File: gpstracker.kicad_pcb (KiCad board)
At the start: 2 copper layers, 79.2 x 59.2 mm, 193 parts, among them IC1 SIM808, J1 Molex 105133-0002, J2 Leds, J3 47553-0001, J4 CONN_COAXIAL, J5 CONN_COAXIAL, J6 Micro_SD_Card, Q1 DMP1045U, SW1 Reset, U1 MCP73832-5-OT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

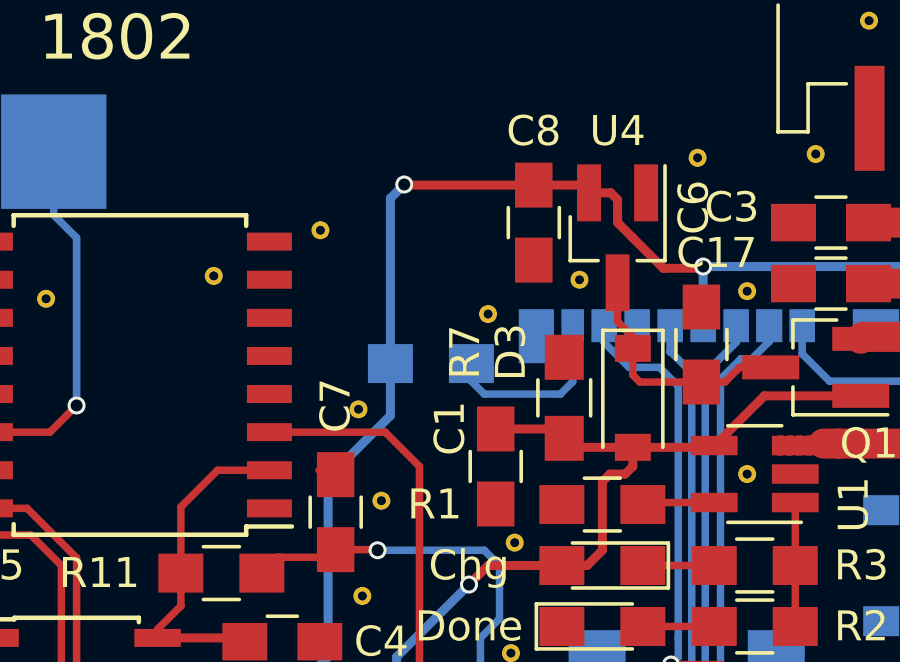
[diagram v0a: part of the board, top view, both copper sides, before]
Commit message: Move sd card right pull up resistor a bit avoid conflicts
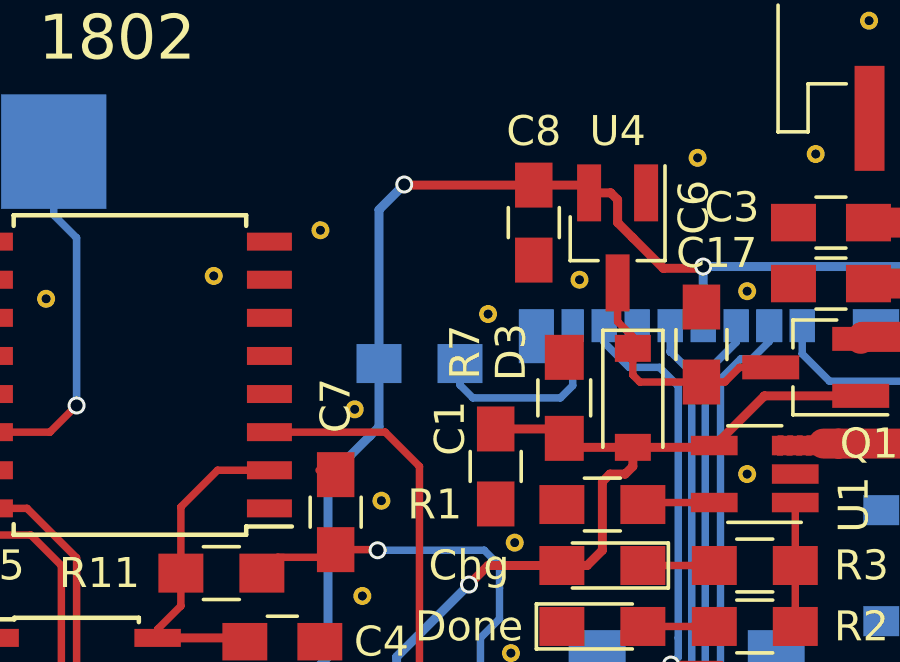
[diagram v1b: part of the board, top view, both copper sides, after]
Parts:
- moved R14 0.38 mm to (123.4, 85.2)
- moved VIA** 0.13 mm to (121.3, 86.7)
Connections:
- J6 pad 9: GND -> (no net)
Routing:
- net Net-(J6-Pad8): track 6.18 -> 6.82 mm
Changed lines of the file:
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@@
 (kicad_pcb (version 4) (host pcbnew 4.0.7)
   (general
-    (links 315)
+    (links 314)
     (no_connects 0)
     (area 76.986002 51.656 194.286 129.599)
     (thickness 1.6)
     (drawings 16)
-    (tracks 607)
+    (tracks 609)
     (zones 0)
     (modules 193)
@@
     (mod_text_size 1 1)
     (mod_text_width 0.15)
-    (pad_size 2.1 2.1)
-    (pad_drill 1.35)
+    (pad_size 1.2 1)
+    (pad_drill 0)
     (pad_to_mask_clearance 0.2)
     (aux_axis_origin 0 0)
@@
     (pad 1 smd rect (at 3.105 -5.2) (size 0.85 1.1) (layers B.Cu B.Paste B.Mask)
       (net 68 "Net-(J6-Pad1)"))
-    (pad 9 smd rect (at 5.74 0.95) (size 1.2 1) (layers B.Cu B.Paste B.Mask)
-      (net 2 GND))
+    (pad 9 smd rect (at 5.74 0.95) (size 1.2 1) (layers B.Cu B.Paste B.Mask))
     (pad 10 smd rect (at 5.74 4.65) (size 1.2 1) (layers B.Cu B.Paste B.Mask))
     (pad G3 smd rect (at -3.73 5.625) (size 1.9 1.35) (layers B.Cu B.Paste B.Mask))
@@
   )
   (module custom-conn:Via-0.6mm (layer F.Cu)
-    (at 121.412 86.741)
+    (at 121.285 86.741)
     (fp_text reference VIA** (at 0 1.27) (layer F.SilkS) hide
       (effects (font (size 1 1) (thickness 0.15)))
@@
   )
   (module Resistors_SMD:R_0805_HandSoldering (layer B.Cu)
-    (at 123.825 85.217 180)
+    (at 123.444 85.217 180)
     (descr "Resistor SMD 0805, hand soldering")
     (tags "resistor 0805")
@@
   (segment (start 129.94 98.366) (end 129.94 96.481) (width 0.25) (layer F.Cu) (net 5))
   (segment (start 129.94 96.481) (end 130.155 96.266) (width 0.25) (layer F.Cu) (net 5))
-  (segment (start 122.475 85.217) (end 122.475 86.948) (width 0.3) (layer B.Cu) (net 6))
-  (segment (start 122.475 86.948) (end 120.396 89.027) (width 0.3) (layer B.Cu) (net 6))
-  (segment (start 122.475 85.217) (end 122.475 79.709) (width 0.3) (layer B.Cu) (net 6))
-  (segment (start 122.475 79.709) (end 122.936 79.248) (width 0.3) (layer B.Cu) (net 6))
+  (segment (start 122.094 85.217) (end 122.094 87.329) (width 0.3) (layer B.Cu) (net 6))
+  (segment (start 122.094 87.329) (end 121.793 87.63) (width 0.3) (layer B.Cu) (net 6))
+  (segment (start 122.094 85.217) (end 122.094 80.09) (width 0.3) (layer B.Cu) (net 6))
+  (segment (start 122.094 80.09) (end 122.936 79.248) (width 0.3) (layer B.Cu) (net 6))
+  (segment (start 122.174 85.137) (end 122.094 85.217) (width 0.3) (layer B.Cu) (net 6))
+  (segment (start 121.793 87.63) (end 120.396 89.027) (width 0.3) (layer B.Cu) (net 6))
+  (segment (start 120.396 94.996) (end 120.396 89.027) (width 0.3) (layer B.Cu) (net 6))
+  (segment (start 118.872 96.52) (end 120.396 94.996) (width 0.3) (layer B.Cu) (net 6))
   (segment (start 132.901 81.983) (end 139.721 81.983) (width 0.3) (layer B.Cu) (net 6))
   (segment (start 139.721 81.983) (end 140.843 83.105) (width 0.3) (layer B.Cu) (net 6))
@@
   (segment (start 130.048 80.518) (end 130.556 81.026) (width 0.3) (layer F.Cu) (net 6))
   (segment (start 122.936 79.248) (end 122.956 79.268) (width 0.3) (layer F.Cu) (net 6))
-  (segment (start 122.956 79.268) (end 127.254 79.268) (width 0.3) (layer F.Cu) (net 6))
   (via (at 122.936 79.248) (size 0.6) (drill 0.4) (layers F.Cu B.Cu) (net 6))
+  (segment (start 122.956 79.268) (end 127.254 79.268) (width 0.3) (layer F.Cu) (net 6))
   (segment (start 124.46 118.03) (end 124.46 115.316) (width 0.3) (layer F.Cu) (net 6))
   (segment (start 126.492 113.284) (end 128.524 113.284) (width 0.3) (layer B.Cu) (net 6))
@@
   (segment (start 137.668 114.808) (end 137.668 113.284) (width 0.3) (layer F.Cu) (net 6))
   (segment (start 143.256 120.396) (end 137.668 114.808) (width 0.3) (layer F.Cu) (net 6))
-  (segment (start 118.872 96.52) (end 120.396 94.996) (width 0.3) (layer B.Cu) (net 6))
-  (segment (start 120.396 94.996) (end 120.396 89.027) (width 0.3) (layer B.Cu) (net 6))
   (segment (start 128.25 109.24) (end 128.25 111.112) (width 0.3) (layer F.Cu) (net 6))
   (segment (start 128.25 111.112) (end 127.856 111.506) (width 0.3) (layer F.Cu) (net 6))
@@
   (segment (start 151.972 118.364) (end 151.972 116.332) (width 0.25) (layer F.Cu) (net 64))
   (segment (start 151.972 120.396) (end 151.972 118.364) (width 0.25) (layer F.Cu) (net 64))
-  (segment (start 125.175 85.217) (end 125.175 85.805) (width 0.25) (layer B.Cu) (net 66))
-  (segment (start 125.175 85.805) (end 125.603 86.233) (width 0.25) (layer B.Cu) (net 66))
-  (segment (start 125.603 86.233) (end 128.143 86.233) (width 0.25) (layer B.Cu) (net 66))
-  (segment (start 128.143 86.233) (end 128.551 85.825) (width 0.25) (layer B.Cu) (net 66))
-  (segment (start 128.551 85.825) (end 128.551 83.954) (width 0.25) (layer B.Cu) (net 66))
+  (segment (start 124.794 85.217) (end 124.794 85.932) (width 0.25) (layer B.Cu) (net 66))
+  (segment (start 128.551 85.952) (end 128.551 83.954) (width 0.25) (layer B.Cu) (net 66))
+  (segment (start 128.143 86.36) (end 128.551 85.952) (width 0.25) (layer B.Cu) (net 66))
+  (segment (start 125.222 86.36) (end 128.143 86.36) (width 0.25) (layer B.Cu) (net 66))
+  (segment (start 124.794 85.932) (end 125.222 86.36) (width 0.25) (layer B.Cu) (net 66))
   (segment (start 133.477 99.312602) (end 133.477 85.736004) (width 0.25) (layer B.Cu) (net 67))
   (segment (start 133.477 85.736004) (end 133.477 85.725) (width 0.25) (layer B.Cu) (net 67))

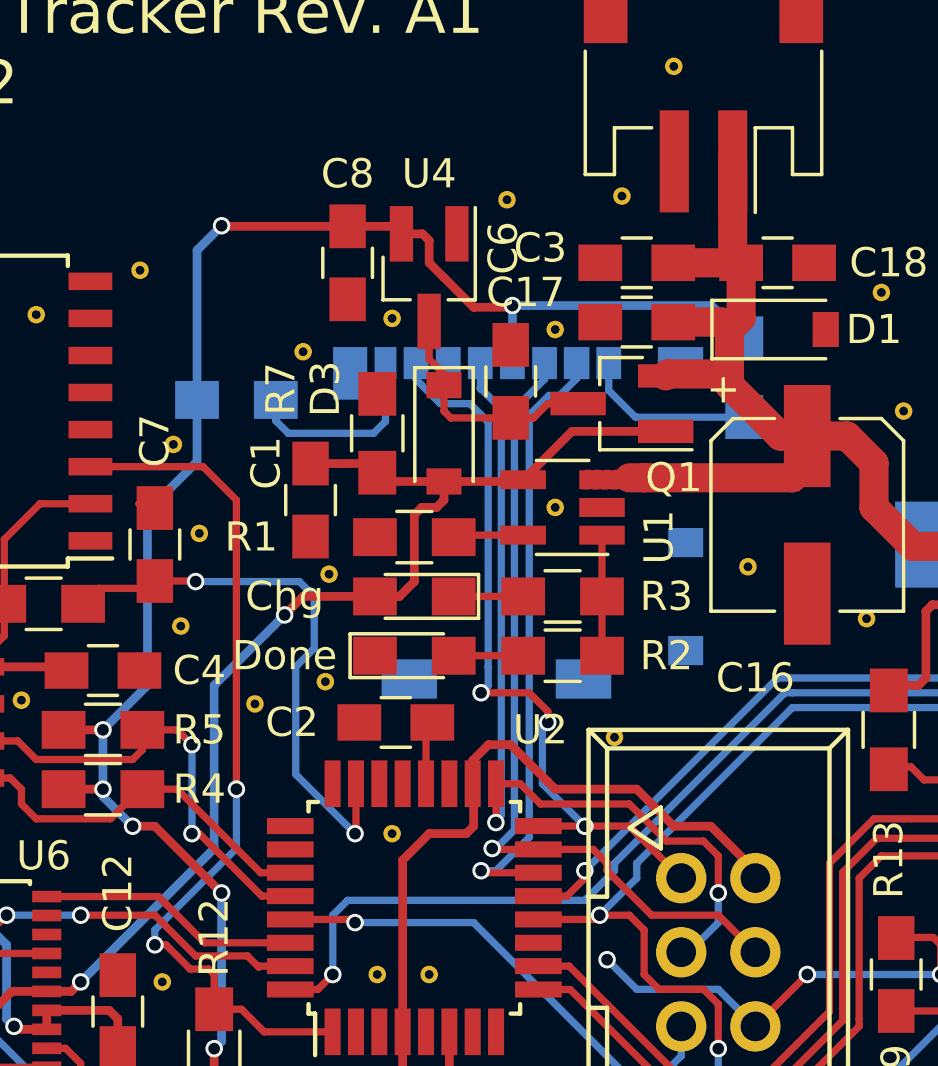
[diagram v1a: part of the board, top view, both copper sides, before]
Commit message: Replaced MOLEX_104031-0811 with cheaper and easier Hirose_DM3AT-SF-PEJM5
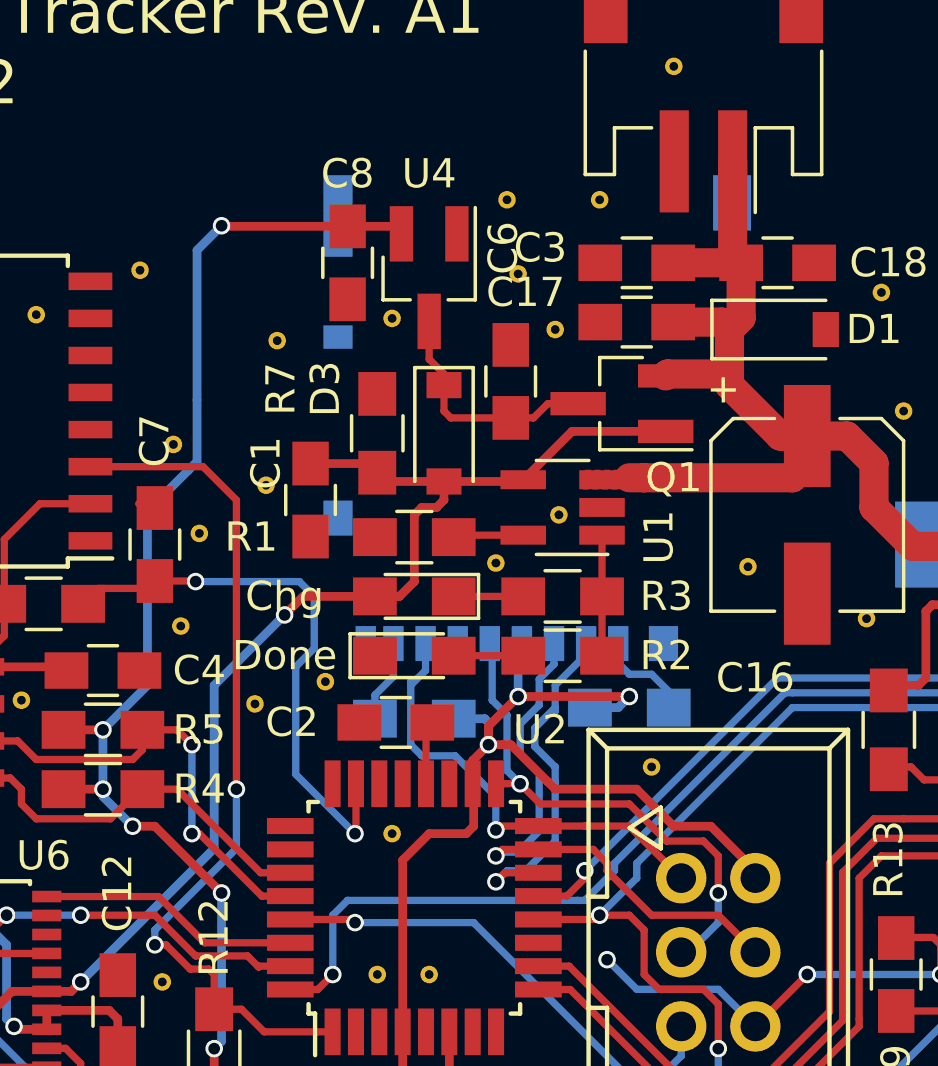
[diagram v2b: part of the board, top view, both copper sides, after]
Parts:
- added VIA**: Via-0.6mm, custom-conn:Via-0.6mm, F.Cu at (132.3, 90.8)
- added VIA**: Via-0.6mm, custom-conn:Via-0.6mm, F.Cu at (133.1, 80.9)
- J6: footprint 104031-0811:MOLEX_104031-0811 -> Connectors_Card:Hirose_DM3AT-SF-PEJM5
- moved R14 12.5 mm to (129.5, 96.1), turned to 0 degrees
- moved R15 12.0 mm to (136.9, 95.8), turned to 180 degrees
- moved J6 5.13 mm to (136.5, 93.0)
- moved VIA** 3.74 mm to (124.5, 88.1)
- moved VIA** 1.63 mm to (137.7, 97.8)
- moved VIA** 0.97 mm to (124.8, 83.2)
- moved VIA** 0.77 mm to (135.9, 78.4)
- moved VIA** 0.28 mm to (134.5, 89.2)
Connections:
- J3 pad GND1: (no net) -> GND
- J3 pad GND2: (no net) -> GND
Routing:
- net /ARD_SCK: track 30.1 -> 17.8 mm
- net /ARD_MISO: track 25.8 -> 15.9 mm, vias 3 -> 1
- net /ARD_IO10: track 21.3 -> 12.2 mm
- net /ARD_MOSI: track 28.2 -> 19.6 mm
- net +3V3: track 128.5 -> 124.4 mm, vias 10 -> 12
- net Net-(J6-Pad8): track 6.82 -> 2.84 mm
- net Net-(J6-Pad1): track 5.96 -> 3.36 mm

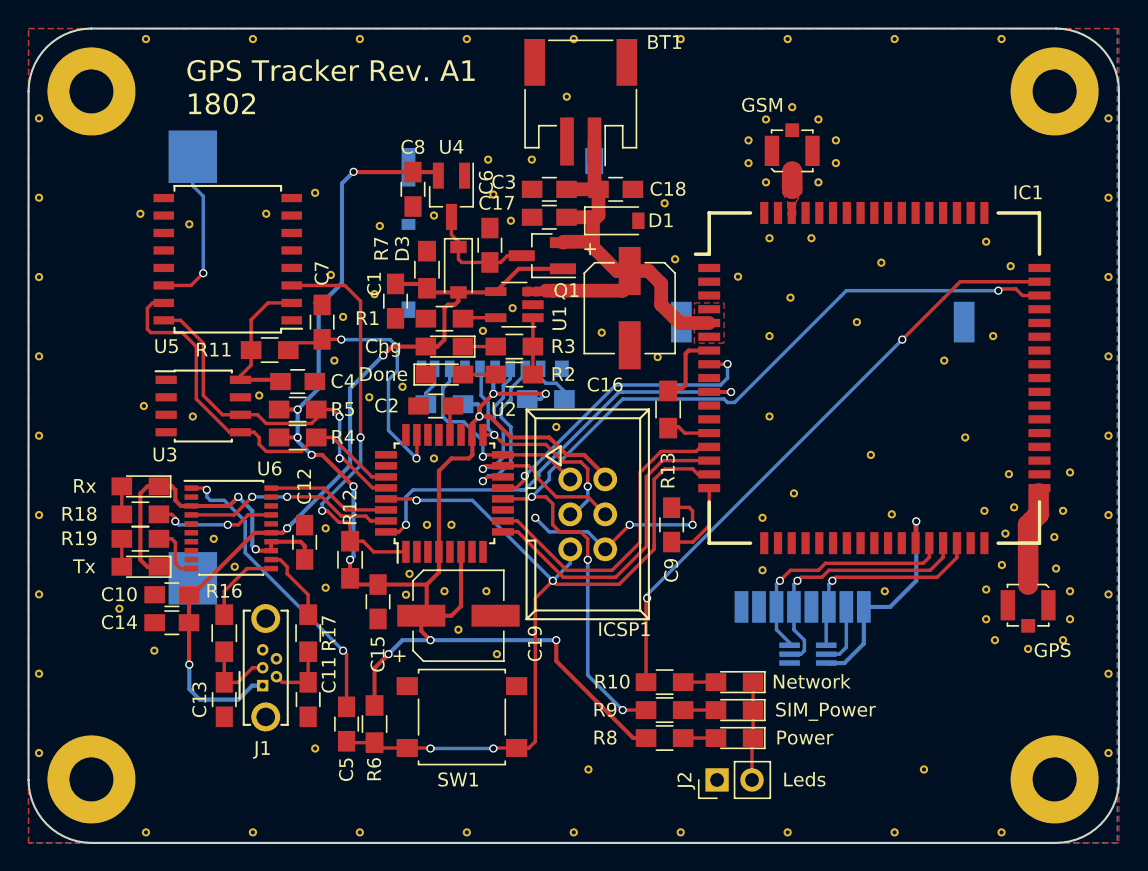
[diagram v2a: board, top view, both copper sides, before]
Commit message: Fix SIM808 reset pin being tied to hardware reset. Fixed ground pads on sdcard
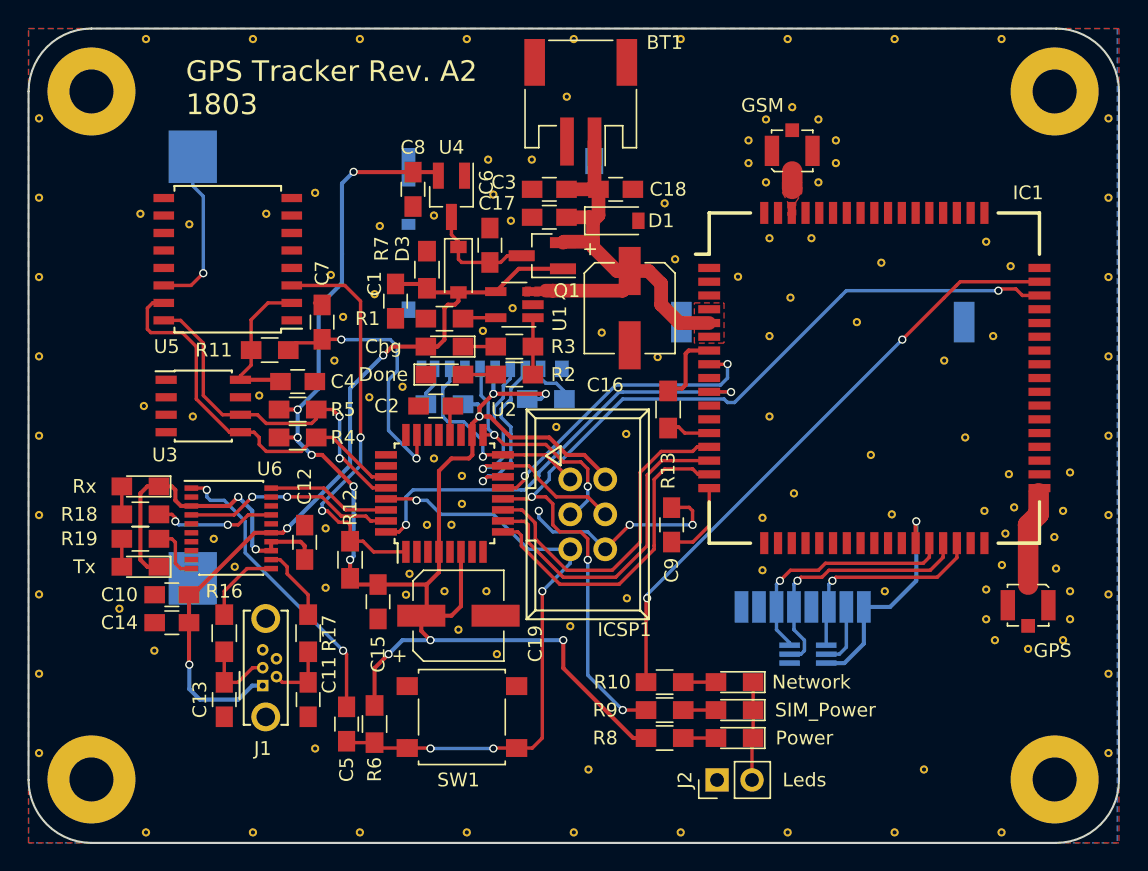
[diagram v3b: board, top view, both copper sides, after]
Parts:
- added VIA**: Via-0.6mm, custom-conn:Via-0.6mm, F.Cu at (142.7, 98.3)
- added VIA**: Via-0.6mm, custom-conn:Via-0.6mm, F.Cu at (130.8, 101.3)
- added VIA**: Via-0.6mm, custom-conn:Via-0.6mm, F.Cu at (130.8, 103.4)
- added VIA**: Via-0.6mm, custom-conn:Via-0.6mm, F.Cu at (142.8, 110.2)
- added VIA**: Via-0.6mm, custom-conn:Via-0.6mm, F.Cu at (138.7, 112.3)
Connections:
- IC1 pad 16: /ARD_RST -> /SIM_RST
- J6 pad 9: (no net) -> Net-(J6-Pad9)
- U2 pad 10: /ARD_HRX -> /ARD_HTX
- U2 pad 11: Net-(U2-Pad11) -> /ARD_HRX
- U2 pad 9: /ARD_HTX -> /SIM_RST
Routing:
- net /SIM_RST: track 0.00 -> 23.6 mm
- net /ARD_RST: track 62.3 -> 44.7 mm
- net /ARD_HRX: track 23.2 -> 24.8 mm
- net /ARD_HTX: track 22.8 -> 24.0 mm
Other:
- board text added: "GPS Tracker Rev. A2 1803"
- board text removed: "GPS Tracker Rev. A1 1802"

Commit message: Made SIM808 pads longer for easier hand soldering
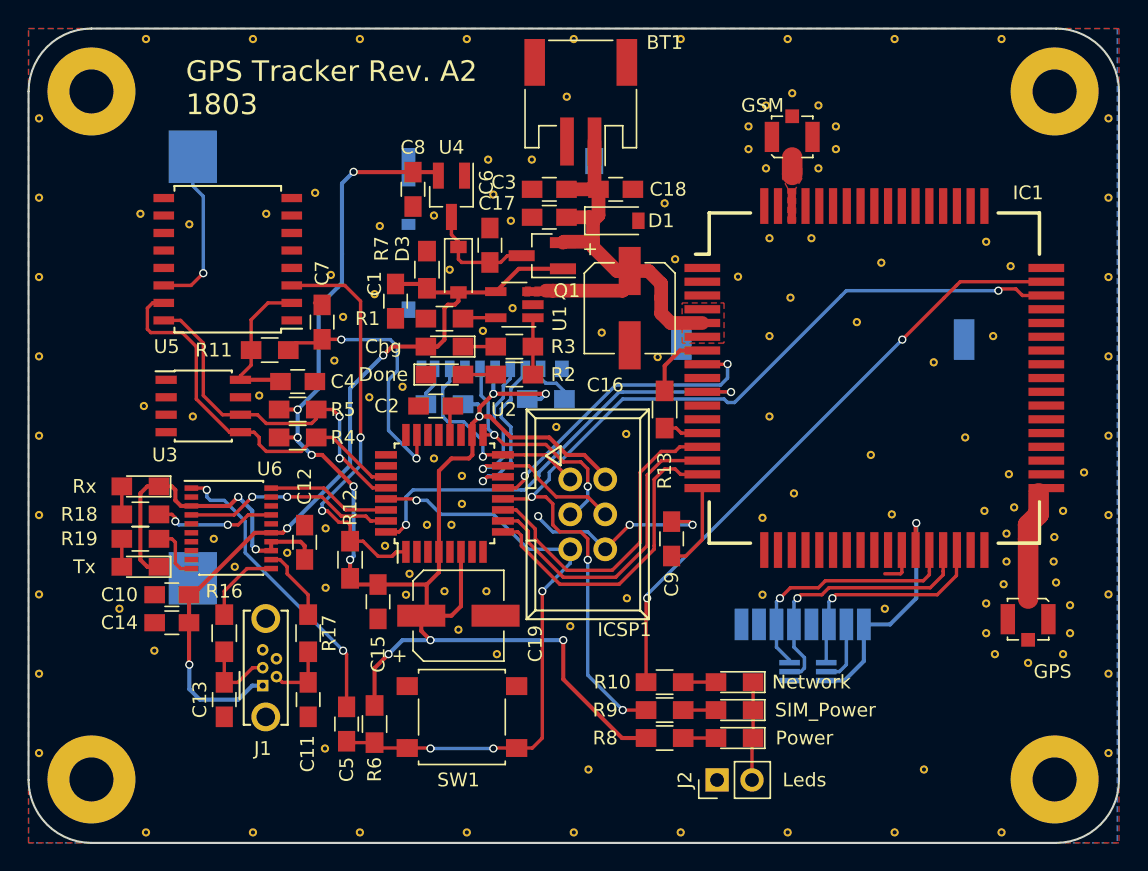
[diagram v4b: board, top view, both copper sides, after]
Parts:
- added VIA**: Via-0.6mm, custom-conn:Via-0.6mm, F.Cu at (129.9, 86.4)
- added VIA**: Via-0.6mm, custom-conn:Via-0.6mm, F.Cu at (118.1, 106.9)
- added VIA**: Via-0.6mm, custom-conn:Via-0.6mm, F.Cu at (125.2, 106.4)
- added VIA**: Via-0.6mm, custom-conn:Via-0.6mm, F.Cu at (170.4, 107.6)
- added VIA**: Via-0.6mm, custom-conn:Via-0.6mm, F.Cu at (173.8, 107.6)
- IC1: footprint SIM808:QFN100P2400X2400X260-68N -> custom-ic:QFN100P2400X2400X260-68N
- moved VIA** 1.78 mm to (152.7, 110.0)
- moved VIA** 1.40 mm to (170.2, 109.2)
- moved VIA** 1.27 mm to (161.5, 111.0)
- moved J3 1.27 mm to (151.1, 91.4)
- moved TV1 1.27 mm to (156.0, 115.6)
- moved C9 1.02 mm to (146.1, 105.9)
- moved J4 1.02 mm to (172.0, 111.8)
- moved J5 1.02 mm to (154.8, 76.7)
- moved VIA** 1.02 mm to (172.0, 114.9)
- moved VIA** 1.02 mm to (152.9, 79.0)
- moved VIA** 1.02 mm to (156.7, 79.0)
- moved VIA** 1.02 mm to (156.7, 74.4)
- moved VIA** 1.02 mm to (158.0, 75.9)
- moved VIA** 1.02 mm to (151.6, 75.9)
- moved VIA** 1.02 mm to (158.0, 77.6)
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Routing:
- net +1V8: track 16.5 -> 18.1 mm
- net GND: track 21.4 -> 22.9 mm
- net +2V8: track 5.30 -> 6.52 mm
- net /GPS: track 7.35 -> 8.37 mm
- net /SIMRST: track 15.7 -> 16.4 mm
- net /WAKE_UP: track 29.9 -> 30.6 mm
- net Net-(C9-Pad1): track 5.95 -> 6.47 mm

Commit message: Fixed LED6 & LED7 being polarity reversed
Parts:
- turned LED6 to 0 degrees
- turned LED7 to 0 degrees
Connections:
- LED6 pad 1: +3V3_FDTI -> Net-(LED6-Pad1)
- LED6 pad 2: Net-(LED6-Pad2) -> +3V3_FDTI
- LED7 pad 1: +3V3_FDTI -> Net-(LED7-Pad1)
- LED7 pad 2: Net-(LED7-Pad2) -> +3V3_FDTI
- R18 pad 2: Net-(LED6-Pad2) -> Net-(LED6-Pad1)
- R19 pad 2: Net-(LED7-Pad2) -> Net-(LED7-Pad1)
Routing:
- net Net-(LED7-Pad2): track 2.03 -> 0.00 mm
- net Net-(LED7-Pad1): track 0.00 -> 2.03 mm
- net Net-(LED6-Pad2): track 2.03 -> 0.00 mm
- net Net-(LED6-Pad1): track 0.00 -> 2.03 mm
